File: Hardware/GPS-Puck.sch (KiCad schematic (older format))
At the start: 16 parts

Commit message: Routing
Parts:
- AE1: renamed from AE?; footprint (none) -> Custom:Antenna_APAE1575R1840BADB1F
- C1, C2, C3, C4, C5, C6, C7, C8: renamed from C?; footprint (none) -> Capacitors:CAPC1608N
- L1, L2: renamed from L?; footprint (none) -> Inductors:INDC1608N
- R1: renamed from R?; value Resistor -> 33k; footprint (none) -> Resistors:RESC1608N
- R2, R3: renamed from R?; footprint (none) -> Resistors:RESC1608N
- U1: renamed from U?; footprint (none) -> Custom:Sensor_Venus838
- U2: renamed from U?; footprint (none) -> SON:SON50P200X200-9T100X180N
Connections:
- net GND: now also U1.10 (GND), U1.11 (GND), U1.15 (GND), U1.19 (GND), U1.4 (GND), U1.49 (GND), U1.5 (GND), U1.6 (GND), U1.60 (GND), U1.64 (GND)
- net GPS4: now reaches C4.1, U1.32 (RFIN)
- net GPS0: now reaches AE1.1, C8.1
- net GPS2: now reaches L2.1, U2.2 (RF_IN)
- net GPS3: now reaches C4.2, L1.2, R2.2, U2.7 (RF_OUT)
- net GPS1: now reaches C8.2, L2.2
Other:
- moved on the sheet: AE1, C8, L2

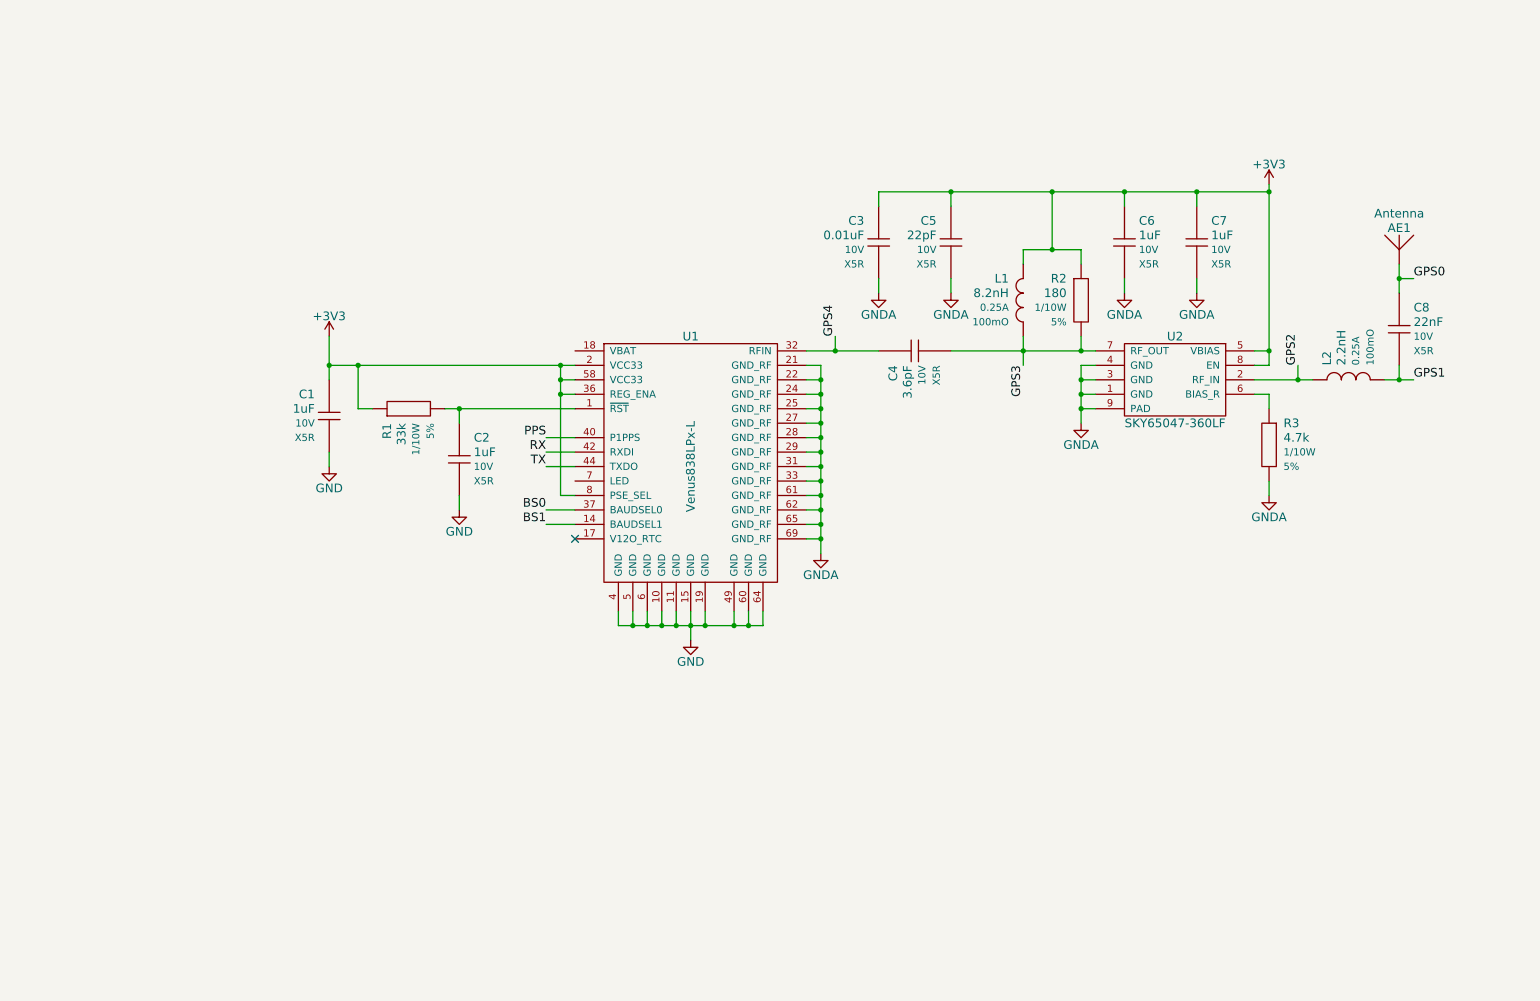
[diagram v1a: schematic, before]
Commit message: Power schematic
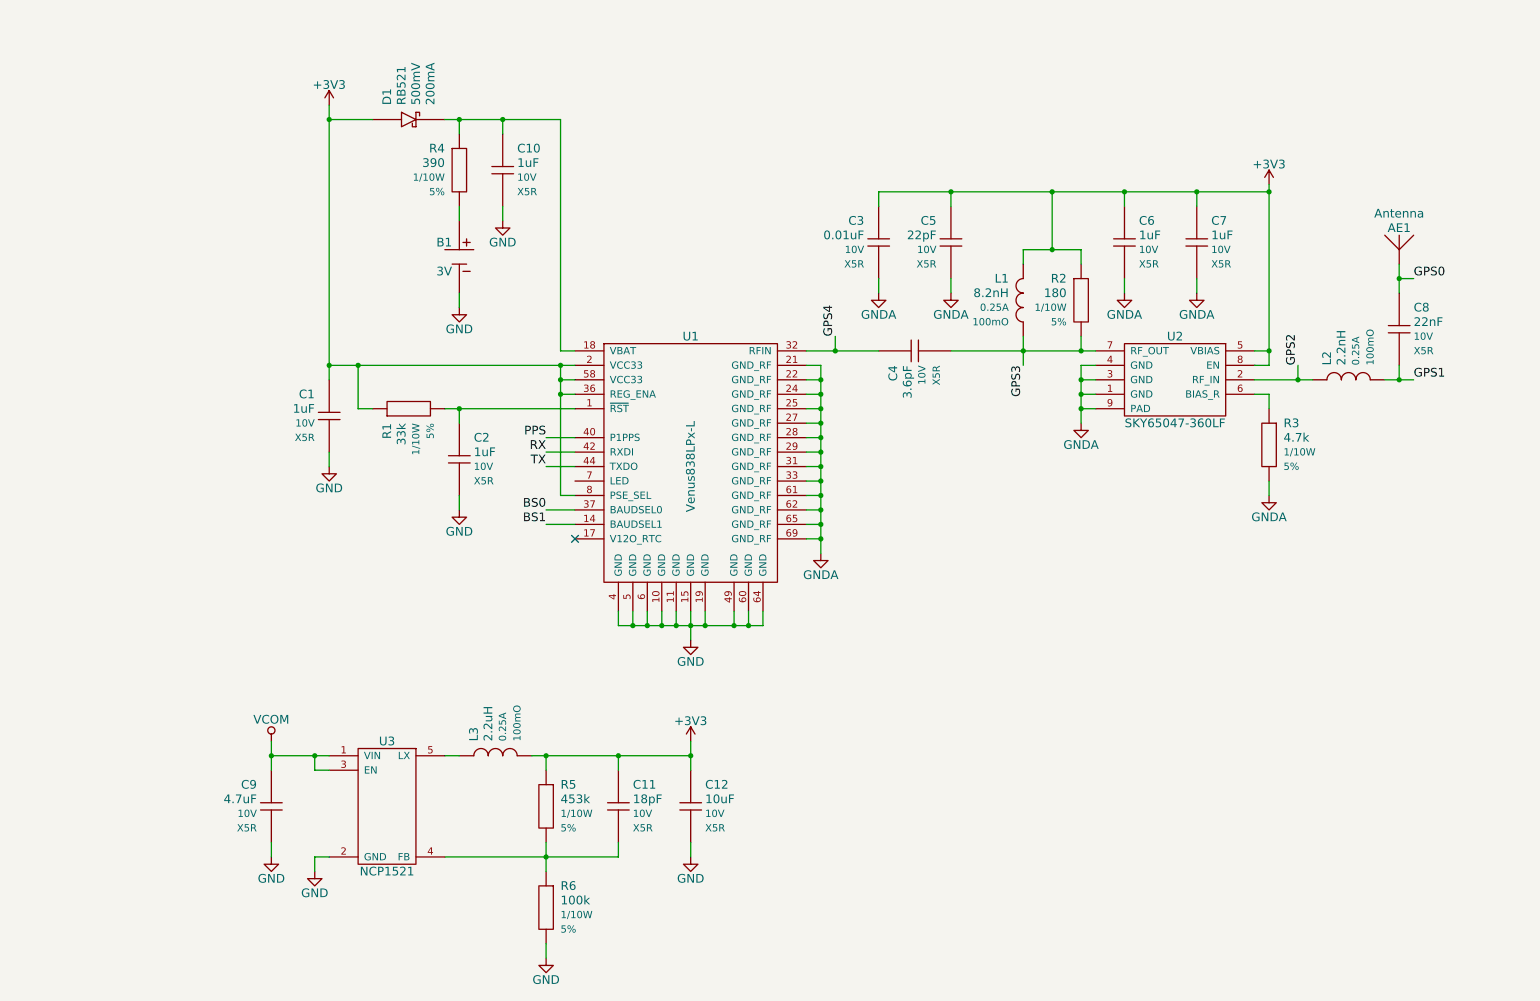
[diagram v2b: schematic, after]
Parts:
- added B1: 3V, Batteries:Battery_ML-1220-F1AN, symbol Battery
- added C10: 1uF, Capacitors:CAPC1608N, symbol Capacitor
- added C11: 18pF, Capacitors:CAPC1608N, symbol Capacitor
- added C12: 10uF, Capacitors:CAPC2012N, symbol Capacitor
- added C9: 4.7uF, Capacitors:CAPC1608N, symbol Capacitor
- added D1: RB521, Diodes:SODFL1608N, symbol Diode-Schottky
- added L3: 2.2uH, Inductors:INDC2012N, symbol Inductor
- added R4: 390, Resistors:RESC1608N, symbol Resistor
- added R5: 453k, Resistors:RESC1608N, symbol Resistor
- added R6: 100k, Resistors:RESC1608N, symbol Resistor
- added U3: NCP1521, SOT:SOT95P275-5L40N, symbol NCP1521
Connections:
- net +3V3: now also C11.1, C12.1, D1.A, L3.2, R5.1
- net GND: now also B1.2, C10.2, C12.2, C9.2, R6.2, U3.2 (GND)
- net at U1.18 (VBAT): now also C10.1, D1.C, R4.1
- new net: C11.2, R5.2, R6.1, U3.4 (FB)
- new net: L3.1, U3.5 (LX)
- new net: B1.1, R4.2
- new net VCOM: C9.1, U3.1 (VIN), U3.3 (EN)

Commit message: Add level translation
Closes #1
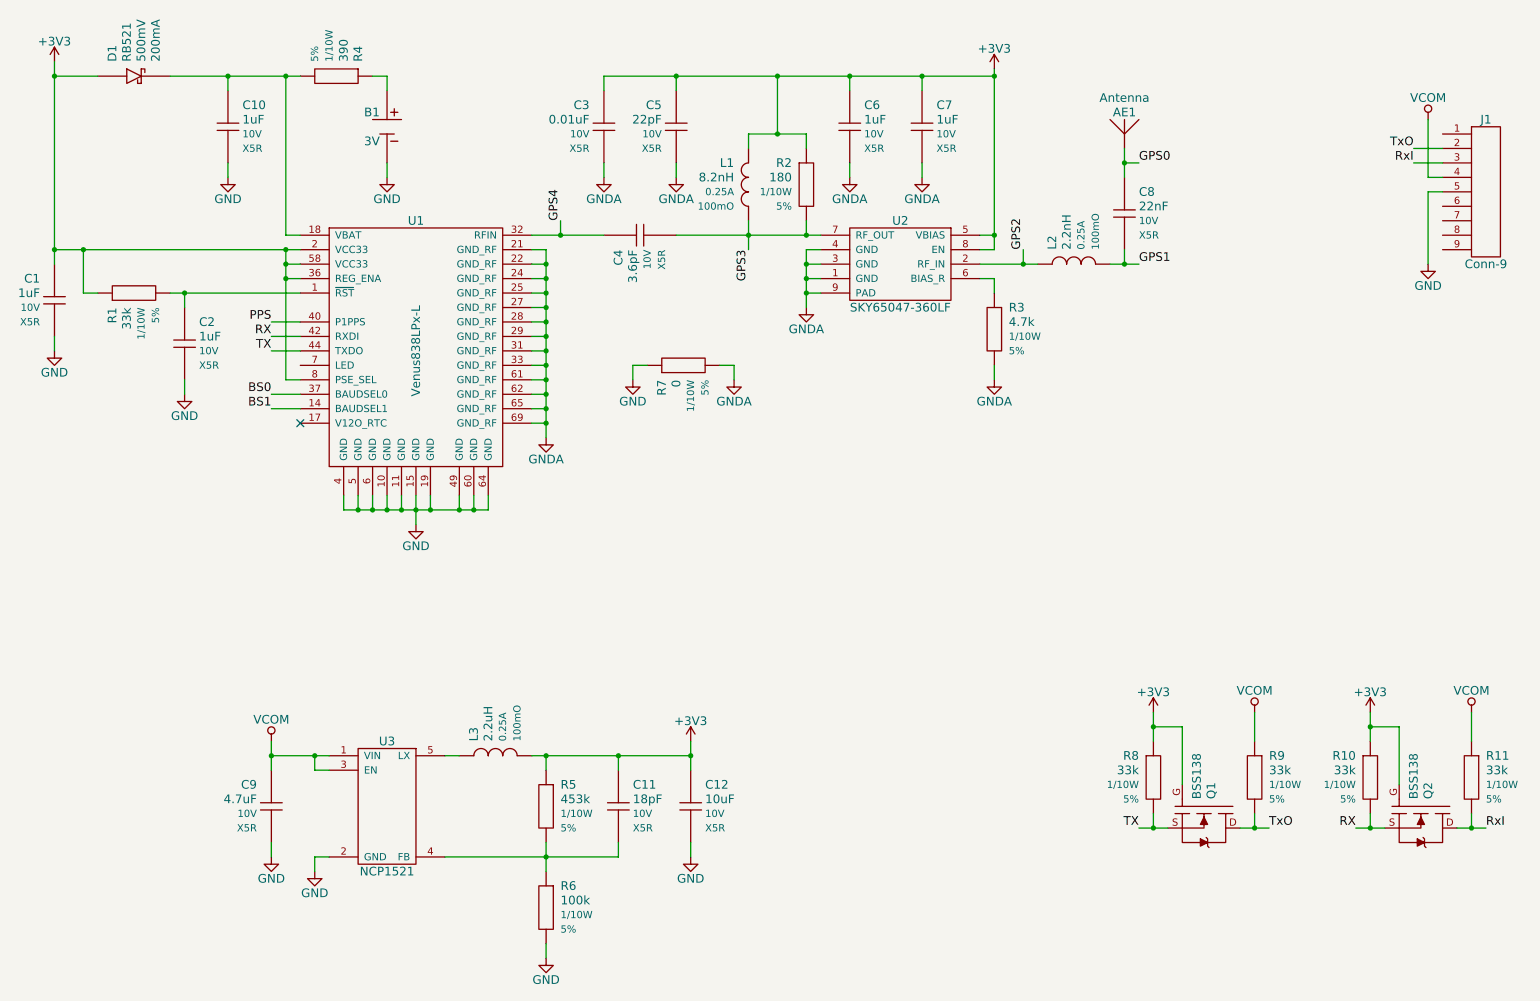
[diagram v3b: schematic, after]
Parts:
- added J1: Conn-9, Connectors:Conn_9-Wire-Pads, symbol Conn-9
- added Q1, Q2: BSS138, SOT:SOT95P240-3N-GSD, symbol MOSFET-N-Body
- added R10, R11, R8, R9: 33k, Resistors:RESC1608N, symbol Resistor
- added R7: 0, Resistors:RESC1608N, symbol Resistor
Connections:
- net +3V3: now also Q1.G, Q2.G, R10.1, R8.1
- net GND: now also J1.5, R7.1
- net GNDA: now also R7.2
- net RX: now also Q2.S, R10.2
- net TX: now also Q1.S, R8.2
- net VCOM: now also J1.4, R11.1, R9.1
- net at C10.1, D1.C, U1.18 (VBAT): now also R4.2; no longer R4.1
- net at B1.1: now also R4.1; no longer R4.2
- new net RxI: J1.3, Q2.D, R11.2
- new net TxO: J1.2, Q1.D, R9.2
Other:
- moved on the sheet: AE1, B1, C1, C10, C2, C3, C4, C5, C6, C7, C8, D1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

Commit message: Add serial inverter
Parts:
- added C13: 1uF, Capacitors:CAPC1608N, symbol Capacitor
- added U4: 74HC2G86, SOP:SOP65P400-8N, symbol 74HC2G86
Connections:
- net +3V3: now also C13.2, U4.8
- net GND: now also C13.1, U4.4
- net RX renamed RxL
- net RxL: now also U4.2; no longer U1.42 (RXDI)
- net TX renamed TxL
- net TxL: now also U4.3; no longer U1.44 (TXDO)
- new net Inv: U4.1, U4.6
- new net Rx: U1.42 (RXDI), U4.7
- new net Tx: U1.44 (TXDO), U4.5

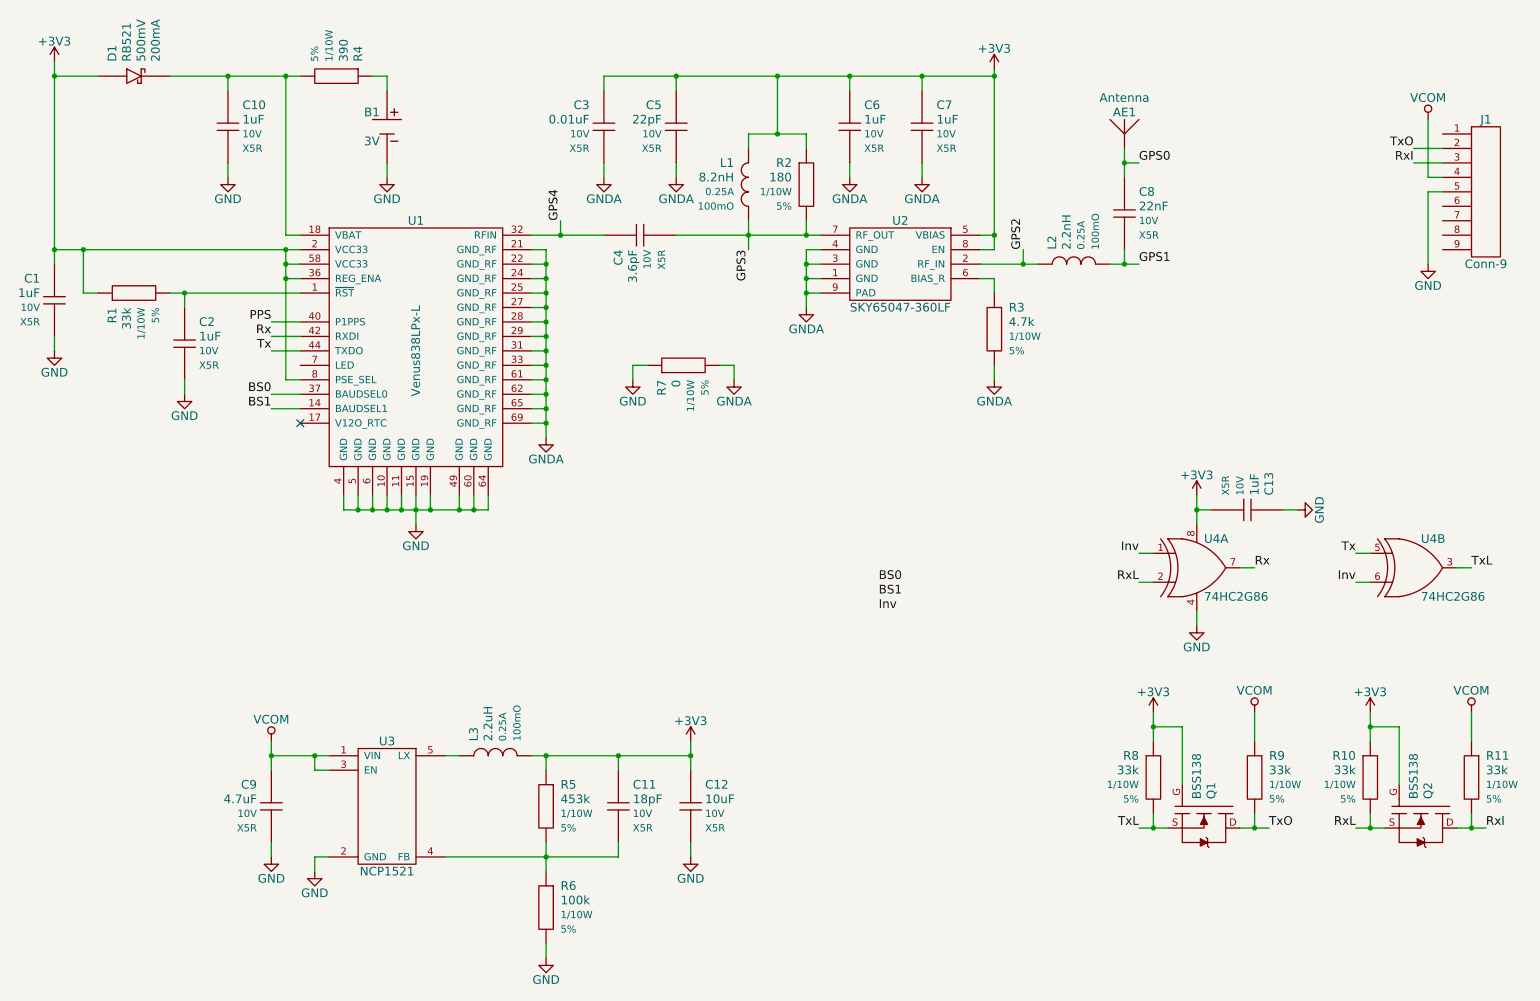
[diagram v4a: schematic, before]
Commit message: Add configuration jumpers
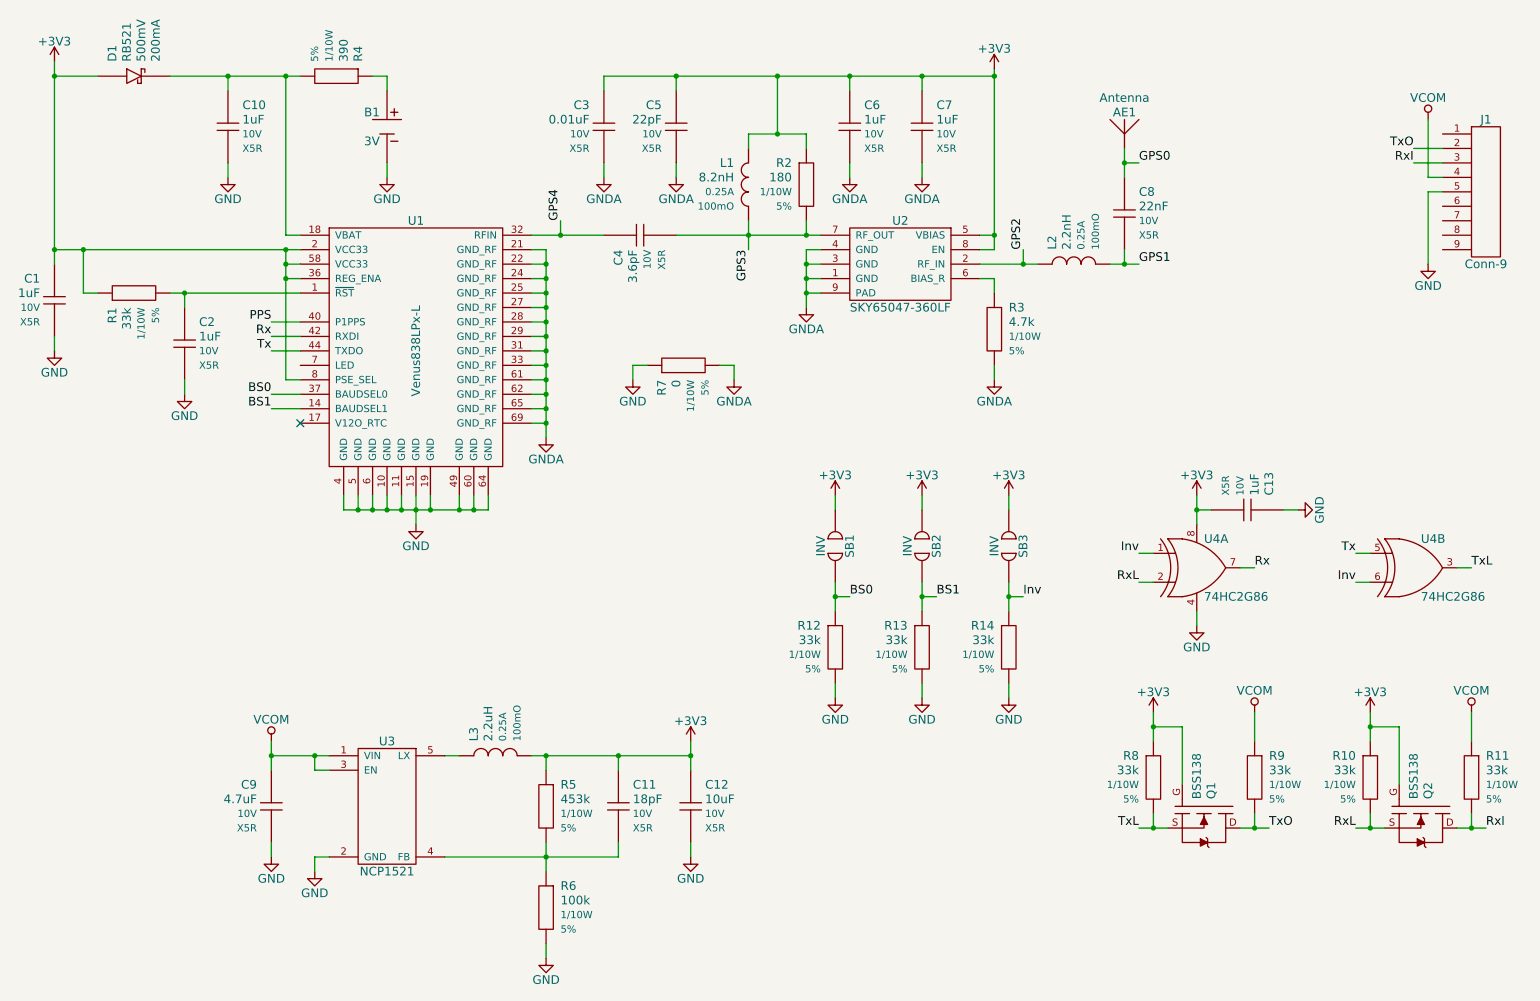
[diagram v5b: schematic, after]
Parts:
- added R12, R13, R14: 33k, Resistors:RESC1608N, symbol Resistor
- added SB1, SB2, SB3: INV, Custom:SB1608N, symbol Solder-Bridge
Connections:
- net +3V3: now also SB1.1, SB2.1, SB3.1
- net BS0: now also R12.1, SB1.2
- net BS1: now also R13.1, SB2.2
- net GND: now also R12.2, R13.2, R14.2
- net Inv: now also R14.1, SB3.2
